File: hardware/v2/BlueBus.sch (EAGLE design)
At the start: 141 parts, among them J1 3PIN_953442_1, J2 6PIN_953442_1, J3 6PIN_5_103166_1, J4 SJ2-35853A-SMT-TR, J5 SMB_CONN, J6 USB3080-30-01-A, J7 PCM12SMTR, J8 TC2030NL, Q1 NMOSFET-BSS138K, Q2 NMOSFET-BSS138K, Q3 PMOSFET-DMP32D4SSOT323, U1 MPQ4420, U10 PCM5122, U11 PAM8406, U2 TH3122.4, U3 FT231XS, U4 S-1212BC0-U5T1U, U5 XC6210, U6 CAT25M01, U7 PIC24FJ1024GA606, U8 BM83SM1, U9 DIT4096

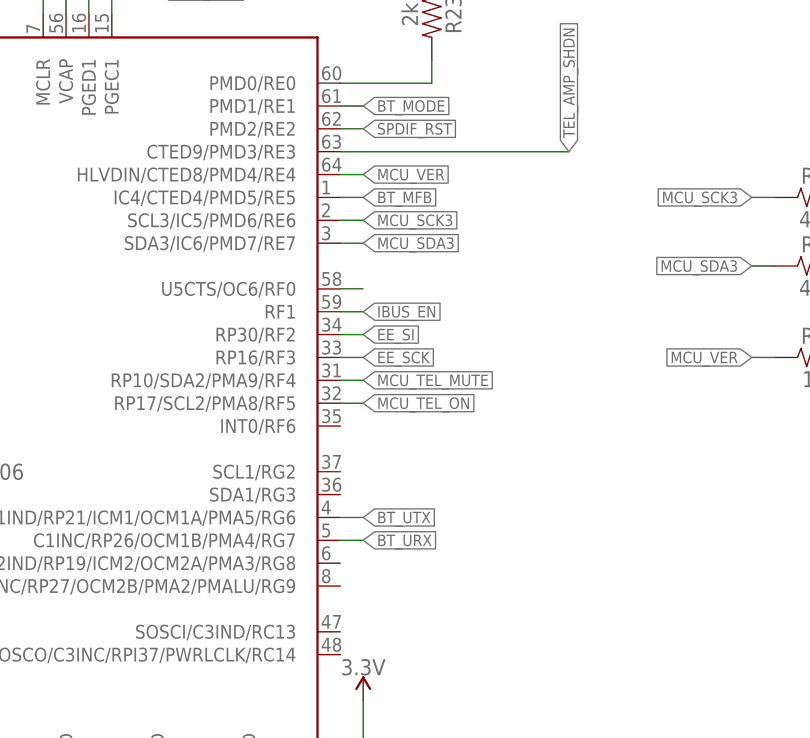
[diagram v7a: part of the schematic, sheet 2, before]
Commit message: [IMP] hardware: v2 Bugfixes * Swap BT UART lines * Move MCU_VER to pin 6 of PIC24 as pin 65 was used in 1.x * Swap MCLK and BCLK on DIT4096 * Add Cutout to board edge for panelization * Add diagonal fiducial
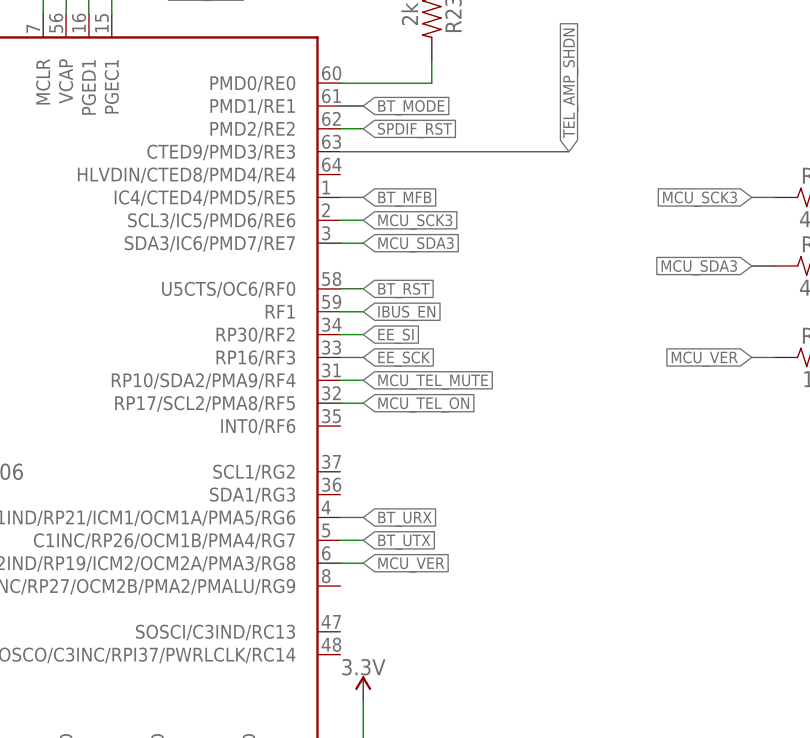
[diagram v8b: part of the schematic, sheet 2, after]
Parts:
- added FID3: FIDUCIAL_1MM, MF_Aesthetics:FIDUCIAL_1MM
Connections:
- removed net I2S_CLK: U10.BCK, U8.SCLK1, U9.MCLK
- removed net I2S_SCK: U10.SCK, U8.MCLK1, U9.SCLK
- new net I2S_BCK: U10.BCK, U8.SCLK1, U9.SCLK
- new net I2S_MCLK: U10.SCK, U8.MCLK1, U9.MCLK
- net BT_URX: now also U7.C1IND/RP21/ICM1/OCM1A/PMA5/RG6; no longer U7.C1INC/RP26/OCM1B/PMA4/RG7
- net BT_UTX: now also U7.C1INC/RP26/OCM1B/PMA4/RG7; no longer U7.C1IND/RP21/ICM1/OCM1A/PMA5/RG6
- net MCU_VER: now also U7.C2IND/RP19/ICM2/OCM2A/PMA3/RG8; no longer U7.HLVDIN/CTED8/PMD4/RE4
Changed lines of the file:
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@@
 <part name="FID1" library="MF_Aesthetics" deviceset="FIDUCIAL" device="_1MM"/>
 <part name="FID2" library="MF_Aesthetics" deviceset="FIDUCIAL" device="_1MM"/>
+<part name="FID3" library="MF_Aesthetics" deviceset="FIDUCIAL" device="_1MM"/>
 </parts>
 <sheets>
@@
 <attribute name="VALUE" x="45.72" y="26.416" size="1.016" layer="96" font="vector" rot="MR180"/>
 <attribute name="NAME" x="45.72" y="27.94" size="1.016" layer="95" font="vector" rot="MR180"/>
+</instance>
+<instance part="FID3" gate="G$1" x="45.72" y="22.86" smashed="yes">
+<attribute name="VALUE" x="45.72" y="21.336" size="1.016" layer="96" font="vector" rot="MR180"/>
+<attribute name="NAME" x="45.72" y="22.86" size="1.016" layer="95" font="vector" rot="MR180"/>
 </instance>
 </instances>
@@
 </segment>
 </net>
-<net name="BT_UTX" class="5">
-<segment>
-<wire x1="170.18" y1="86.36" x2="172.72" y2="86.36" width="0.1524" layer="91"/>
-<label x="172.72" y="86.36" size="1.27" layer="95" xref="yes"/>
-<pinref part="U7" gate="G$1" pin="C1IND/RP21/ICM1/OCM1A/PMA5/RG6"/>
-</segment>
-</net>
-<net name="BT_URX" class="5">
-<segment>
-<wire x1="170.18" y1="83.82" x2="172.72" y2="83.82" width="0.1524" layer="91"/>
-<label x="172.72" y="83.82" size="1.27" layer="95" xref="yes"/>
-<pinref part="U7" gate="G$1" pin="C1INC/RP26/OCM1B/PMA4/RG7"/>
-</segment>
-</net>
 <net name="3.3V" class="2">
 <segment>
@@
 <pinref part="U7" gate="G$1" pin="U5CTS/OC6/RF0"/>
 <wire x1="170.18" y1="111.76" x2="172.72" y2="111.76" width="0.1524" layer="91"/>
+<label x="172.72" y="111.76" size="1.27" layer="95" xref="yes"/>
 </segment>
 </net>
@@
 <net name="MCU_VER" class="0">
 <segment>
-<pinref part="U7" gate="G$1" pin="HLVDIN/CTED8/PMD4/RE4"/>
-<wire x1="170.18" y1="124.46" x2="172.72" y2="124.46" width="0.1524" layer="91"/>
-<label x="172.72" y="124.46" size="1.27" layer="95" xref="yes"/>
-</segment>
-<segment>
 <pinref part="R19" gate="G$1" pin="1"/>
 <wire x1="218.44" y1="104.14" x2="215.9" y2="104.14" width="0.1524" layer="91"/>
 <label x="215.9" y="104.14" size="1.27" layer="95" rot="R180" xref="yes"/>
+</segment>
+<segment>
+<pinref part="U7" gate="G$1" pin="C2IND/RP19/ICM2/OCM2A/PMA3/RG8"/>
+<wire x1="170.18" y1="81.28" x2="172.72" y2="81.28" width="0.1524" layer="91"/>
+<label x="172.72" y="81.28" size="1.27" layer="95" xref="yes"/>
 </segment>
 </net>
@@
 <pinref part="U7" gate="G$1" pin="RP23/PMACK1/RD2"/>
 <wire x1="40.64" y1="83.82" x2="40.64" y2="78.74" width="0.1524" layer="91"/>
+</segment>
+</net>
+<net name="BT_URX" class="5">
+<segment>
+<pinref part="U7" gate="G$1" pin="C1IND/RP21/ICM1/OCM1A/PMA5/RG6"/>
+<wire x1="170.18" y1="86.36" x2="172.72" y2="86.36" width="0.1524" layer="91"/>
+<label x="172.72" y="86.36" size="1.27" layer="95" xref="yes"/>
+</segment>
+</net>
+<net name="BT_UTX" class="5">
+<segment>
+<pinref part="U7" gate="G$1" pin="C1INC/RP26/OCM1B/PMA4/RG7"/>
+<wire x1="170.18" y1="83.82" x2="172.72" y2="83.82" width="0.1524" layer="91"/>
+<label x="172.72" y="83.82" size="1.27" layer="95" xref="yes"/>
 </segment>
 </net>
@@
 </segment>
 </net>
-<net name="I2S_SCK" class="0">
+<net name="I2S_MCLK" class="0">
 <segment>
 <pinref part="U8" gate="G$1" pin="MCLK1"/>
@@
 </segment>
 </net>
-<net name="I2S_CLK" class="0">
+<net name="I2S_BCK" class="0">
 <segment>
 <pinref part="U8" gate="G$1" pin="SCLK1"/>
@@
 </segment>
 </net>
-<net name="I2S_CLK" class="0">
+<net name="I2S_BCK" class="0">
 <segment>
 <wire x1="27.94" y1="142.24" x2="25.4" y2="142.24" width="0.1524" layer="91"/>
@@
 </segment>
 <segment>
-<pinref part="U9" gate="G$1" pin="MCLK"/>
-<wire x1="172.72" y1="109.22" x2="170.18" y2="109.22" width="0.1524" layer="91"/>
-<label x="170.18" y="109.22" size="1.27" layer="95" rot="R180" xref="yes"/>
+<pinref part="U9" gate="G$1" pin="SCLK"/>
+<wire x1="172.72" y1="149.86" x2="170.18" y2="149.86" width="0.1524" layer="91"/>
+<label x="170.18" y="149.86" size="1.27" layer="95" rot="R180" xref="yes"/>
 </segment>
 </net>
@@
 </segment>
 </net>
-<net name="I2S_SCK" class="0">
+<net name="I2S_MCLK" class="0">
 <segment>
 <wire x1="27.94" y1="144.78" x2="25.4" y2="144.78" width="0.1524" layer="91"/>
@@
 </segment>
 <segment>
-<pinref part="U9" gate="G$1" pin="SCLK"/>
-<wire x1="172.72" y1="149.86" x2="170.18" y2="149.86" width="0.1524" layer="91"/>
-<label x="170.18" y="149.86" size="1.27" layer="95" rot="R180" xref="yes"/>
-</segment>
-</net>
+<pinref part="U9" gate="G$1" pin="MCLK"/>
+<wire x1="172.72" y1="109.22" x2="170.18" y2="109.22" width="0.1524" layer="91"/>
+<label x="170.18" y="109.22" size="1.27" layer="95" rot="R180" xref="yes"/>
+</segment>
+</net>
